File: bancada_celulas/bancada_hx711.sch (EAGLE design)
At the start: 17 parts

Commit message: KK connectors changed from 4mm to 2.54mm
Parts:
- X1, X11, X2, X3, X4, X5: value (none) -> 22-23-2041; device con-molex:KK-156-4 -> con-molex:22-23-2041
- X10, X6, X7, X8, X9: value (none) -> 22-23-2021; device con-molex:KK-156-2 -> con-molex:22-23-2021
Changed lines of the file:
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@@
 <grid distance="0.1" unitdist="inch" unit="inch" style="lines" multiple="1" display="no" altdistance="0.01" altunitdist="inch" altunit="inch"/>
 <layers>
-<layer number="1" name="Top" color="4" fill="1" visible="no" active="no"/>
-<layer number="2" name="Route2" color="1" fill="3" visible="no" active="no"/>
-<layer number="3" name="Route3" color="4" fill="3" visible="no" active="no"/>
-<layer number="4" name="Route4" color="1" fill="4" visible="no" active="no"/>
-<layer number="5" name="Route5" color="4" fill="4" visible="no" active="no"/>
-<layer number="6" name="Route6" color="1" fill="8" visible="no" active="no"/>
-<layer number="7" name="Route7" color="4" fill="8" visible="no" active="no"/>
-<layer number="8" name="Route8" color="1" fill="2" visible="no" active="no"/>
-<layer number="9" name="Route9" color="4" fill="2" visible="no" active="no"/>
-<layer number="10" name="Route10" color="1" fill="7" visible="no" active="no"/>
-<layer number="11" name="Route11" color="4" fill="7" visible="no" active="no"/>
-<layer number="12" name="Route12" color="1" fill="5" visible="no" active="no"/>
-<layer number="13" name="Route13" color="4" fill="5" visible="no" active="no"/>
-<layer number="14" name="Route14" color="1" fill="6" visible="no" active="no"/>
-<layer number="15" name="Route15" color="4" fill="6" visible="no" active="no"/>
-<layer number="16" name="Bottom" color="1" fill="1" visible="no" active="no"/>
-<layer number="17" name="Pads" color="2" fill="1" visible="no" active="no"/>
-<layer number="18" name="Vias" color="2" fill="1" visible="no" active="no"/>
-<layer number="19" name="Unrouted" color="6" fill="1" visible="no" active="no"/>
-<layer number="20" name="Dimension" color="15" fill="1" visible="no" active="no"/>
-<layer number="21" name="tPlace" color="7" fill="1" visible="no" active="no"/>
-<layer number="22" name="bPlace" color="7" fill="1" visible="no" active="no"/>
-<layer number="23" name="tOrigins" color="15" fill="1" visible="no" active="no"/>
-<layer number="24" name="bOrigins" color="15" fill="1" visible="no" active="no"/>
-<layer number="25" name="tNames" color="7" fill="1" visible="no" active="no"/>
-<layer number="26" name="bNames" color="7" fill="1" visible="no" active="no"/>
-<layer number="27" name="tValues" color="7" fill="1" visible="no" active="no"/>
-<layer number="28" name="bValues" color="7" fill="1" visible="no" active="no"/>
+<layer number="1" name="Top" color="4" fill="1" visible="yes" active="no"/>
+<layer number="2" name="Route2" color="1" fill="3" visible="yes" active="no"/>
+<layer number="3" name="Route3" color="4" fill="3" visible="yes" active="no"/>
+<layer number="4" name="Route4" color="1" fill="4" visible="yes" active="no"/>
+<layer number="5" name="Route5" color="4" fill="4" visible="yes" active="no"/>
+<layer number="6" name="Route6" color="1" fill="8" visible="yes" active="no"/>
+<layer number="7" name="Route7" color="4" fill="8" visible="yes" active="no"/>
+<layer number="8" name="Route8" color="1" fill="2" visible="yes" active="no"/>
+<layer number="9" name="Route9" color="4" fill="2" visible="yes" active="no"/>
+<layer number="10" name="Route10" color="1" fill="7" visible="yes" active="no"/>
+<layer number="11" name="Route11" color="4" fill="7" visible="yes" active="no"/>
+<layer number="12" name="Route12" color="1" fill="5" visible="yes" active="no"/>
+<layer number="13" name="Route13" color="4" fill="5" visible="yes" active="no"/>
+<layer number="14" name="Route14" color="1" fill="6" visible="yes" active="no"/>
+<layer number="15" name="Route15" color="4" fill="6" visible="yes" active="no"/>
+<layer number="16" name="Bottom" color="1" fill="1" visible="yes" active="no"/>
+<layer number="17" name="Pads" color="2" fill="1" visible="yes" active="no"/>
+<layer number="18" name="Vias" color="2" fill="1" visible="yes" active="no"/>
+<layer number="19" name="Unrouted" color="6" fill="1" visible="yes" active="no"/>
+<layer number="20" name="Dimension" color="24" fill="1" visible="yes" active="no"/>
+<layer number="21" name="tPlace" color="7" fill="1" visible="yes" active="no"/>
+<layer number="22" name="bPlace" color="7" fill="1" visible="yes" active="no"/>
+<layer number="23" name="tOrigins" color="15" fill="1" visible="yes" active="no"/>
+<layer number="24" name="bOrigins" color="15" fill="1" visible="yes" active="no"/>
+<layer number="25" name="tNames" color="7" fill="1" visible="yes" active="no"/>
+<layer number="26" name="bNames" color="7" fill="1" visible="yes" active="no"/>
+<layer number="27" name="tValues" color="7" fill="1" visible="yes" active="no"/>
+<layer number="28" name="bValues" color="7" fill="1" visible="yes" active="no"/>
 <layer number="29" name="tStop" color="7" fill="3" visible="no" active="no"/>
 <layer number="30" name="bStop" color="7" fill="6" visible="no" active="no"/>
@@
 <layer number="35" name="tGlue" color="7" fill="4" visible="no" active="no"/>
 <layer number="36" name="bGlue" color="7" fill="5" visible="no" active="no"/>
-<layer number="37" name="tTest" color="7" fill="1" visible="no" active="no"/>
-<layer number="38" name="bTest" color="7" fill="1" visible="no" active="no"/>
+<layer number="37" name="tTest" color="7" fill="1" visible="yes" active="no"/>
+<layer number="38" name="bTest" color="7" fill="1" visible="yes" active="no"/>
 <layer number="39" name="tKeepout" color="4" fill="11" visible="no" active="no"/>
 <layer number="40" name="bKeepout" color="1" fill="11" visible="no" active="no"/>
@@
 <layer number="44" name="Drills" color="7" fill="1" visible="no" active="no"/>
 <layer number="45" name="Holes" color="7" fill="1" visible="no" active="no"/>
-<layer number="46" name="Milling" color="3" fill="1" visible="no" active="no"/>
-<layer number="47" name="Measures" color="7" fill="1" visible="no" active="no"/>
-<layer number="48" name="Document" color="7" fill="1" visible="no" active="no"/>
-<layer number="49" name="Reference" color="7" fill="1" visible="no" active="no"/>
-<layer number="51" name="tDocu" color="7" fill="1" visible="no" active="no"/>
-<layer number="52" name="bDocu" color="7" fill="1" visible="no" active="no"/>
+<layer number="46" name="Milling" color="3" fill="1" visible="yes" active="no"/>
+<layer number="47" name="Measures" color="7" fill="1" visible="yes" active="no"/>
+<layer number="48" name="Document" color="7" fill="1" visible="yes" active="no"/>
+<layer number="49" name="Reference" color="7" fill="1" visible="yes" active="no"/>
+<layer number="51" name="tDocu" color="7" fill="1" visible="yes" active="no"/>
+<layer number="52" name="bDocu" color="7" fill="1" visible="yes" active="no"/>
 <layer number="88" name="SimResults" color="9" fill="1" visible="yes" active="yes"/>
 <layer number="89" name="SimProbes" color="9" fill="1" visible="yes" active="yes"/>
@@
 <part name="U$5" library="HX711" deviceset="HX711-1" device=""/>
 <part name="U$6" library="HX711" deviceset="HX711-1" device=""/>
-<part name="X1" library="con-molex" library_urn="urn:adsk.eagle:library:165" deviceset="KK-156-4" device=""/>
-<part name="X2" library="con-molex" library_urn="urn:adsk.eagle:library:165" deviceset="KK-156-4" device=""/>
-<part name="X3" library="con-molex" library_urn="urn:adsk.eagle:library:165" deviceset="KK-156-4" device=""/>
-<part name="X4" library="con-molex" library_urn="urn:adsk.eagle:library:165" deviceset="KK-156-4" device=""/>
-<part name="X5" library="con-molex" library_urn="urn:adsk.eagle:library:165" deviceset="KK-156-4" device=""/>
-<part name="X6" library="con-molex" library_urn="urn:adsk.eagle:library:165" deviceset="KK-156-2" device=""/>
-<part name="X7" library="con-molex" library_urn="urn:adsk.eagle:library:165" deviceset="KK-156-2" device=""/>
-<part name="X8" library="con-molex" library_urn="urn:adsk.eagle:library:165" deviceset="KK-156-2" device=""/>
-<part name="X9" library="con-molex" library_urn="urn:adsk.eagle:library:165" deviceset="KK-156-2" device=""/>
-<part name="X10" library="con-molex" library_urn="urn:adsk.eagle:library:165" deviceset="KK-156-2" device=""/>
+<part name="X1" library="con-molex" library_urn="urn:adsk.eagle:library:165" deviceset="22-23-2041" device=""/>
+<part name="X2" library="con-molex" library_urn="urn:adsk.eagle:library:165" deviceset="22-23-2041" device=""/>
+<part name="X3" library="con-molex" library_urn="urn:adsk.eagle:library:165" deviceset="22-23-2041" device=""/>
+<part name="X4" library="con-molex" library_urn="urn:adsk.eagle:library:165" deviceset="22-23-2041" device=""/>
+<part name="X5" library="con-molex" library_urn="urn:adsk.eagle:library:165" deviceset="22-23-2041" device=""/>
+<part name="X6" library="con-molex" library_urn="urn:adsk.eagle:library:165" deviceset="22-23-2021" device=""/>
+<part name="X7" library="con-molex" library_urn="urn:adsk.eagle:library:165" deviceset="22-23-2021" device=""/>
+<part name="X8" library="con-molex" library_urn="urn:adsk.eagle:library:165" deviceset="22-23-2021" device=""/>
+<part name="X9" library="con-molex" library_urn="urn:adsk.eagle:library:165" deviceset="22-23-2021" device=""/>
+<part name="X10" library="con-molex" library_urn="urn:adsk.eagle:library:165" deviceset="22-23-2021" device=""/>
 <part name="GND7" library="supply1" library_urn="urn:adsk.eagle:library:371" deviceset="GND" device=""/>
 <part name="GND8" library="supply1" library_urn="urn:adsk.eagle:library:371" deviceset="GND" device=""/>
@@
 <part name="P+7" library="supply1" library_urn="urn:adsk.eagle:library:371" deviceset="VCC" device=""/>
 <part name="GND12" library="supply1" library_urn="urn:adsk.eagle:library:371" deviceset="GND" device=""/>
-<part name="X11" library="con-molex" library_urn="urn:adsk.eagle:library:165" deviceset="KK-156-4" device=""/>
+<part name="X11" library="con-molex" library_urn="urn:adsk.eagle:library:165" deviceset="22-23-2041" device=""/>
 </parts>
 <sheets>

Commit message: Name A4 and A5 lines
A4 and A5 lines were hardwired. They are now named A4 and A5.
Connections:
- net N$21 renamed A5
- net N$22 renamed A4
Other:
- moved on the sheet: X11-1, X11-2, X11-3, X11-4

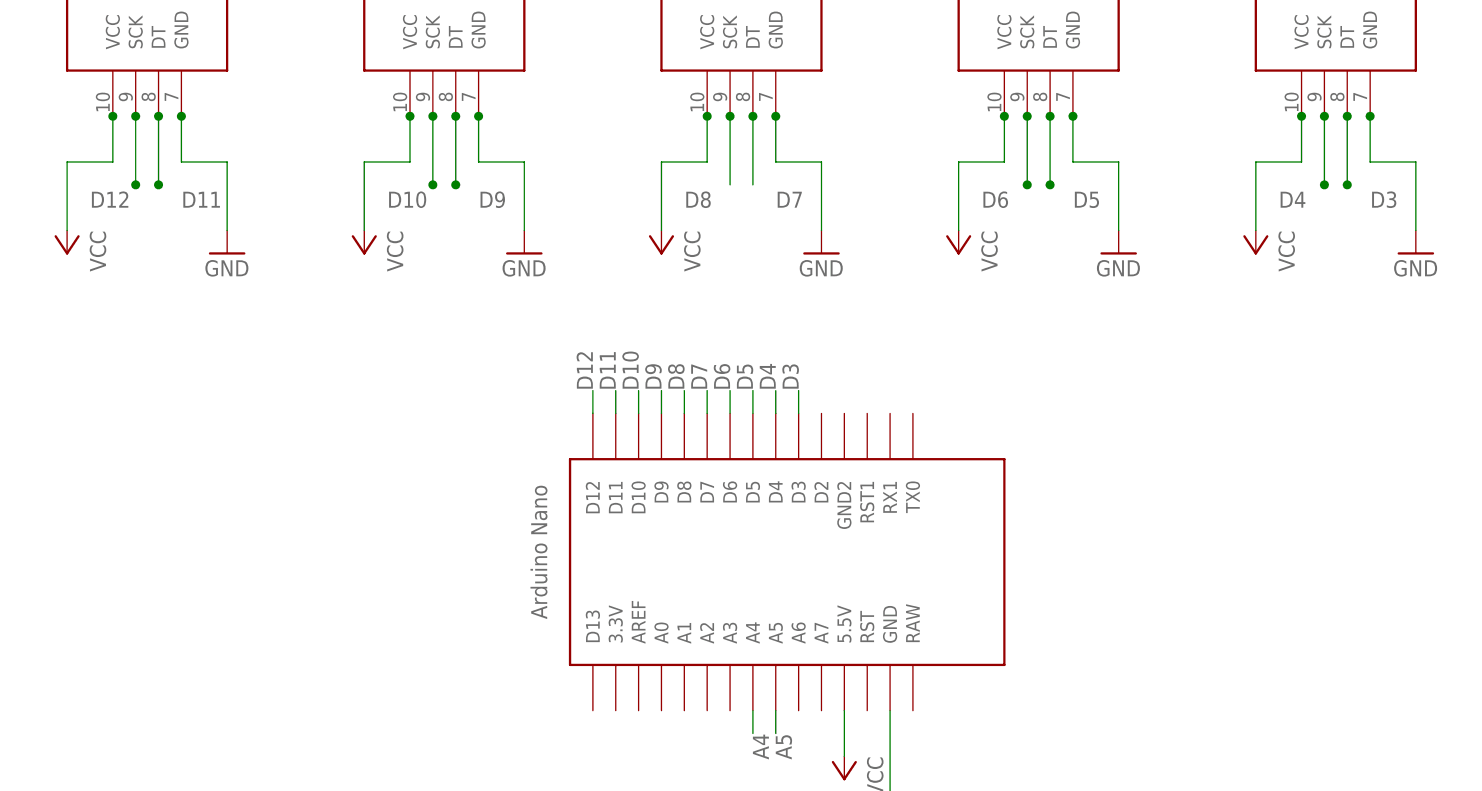
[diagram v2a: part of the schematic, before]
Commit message: Add jumpers (or 0ohm resistors)
In previous design, some ground planes were unconnected to each other. It was meant to be added jumper wires after production.

This commit changes this to actual jumpers, with pins, so they don't need to be soldered from bottom, but can actually be placed on top, like any other through-hole component. 0ohm through-hole resistors can also be used.
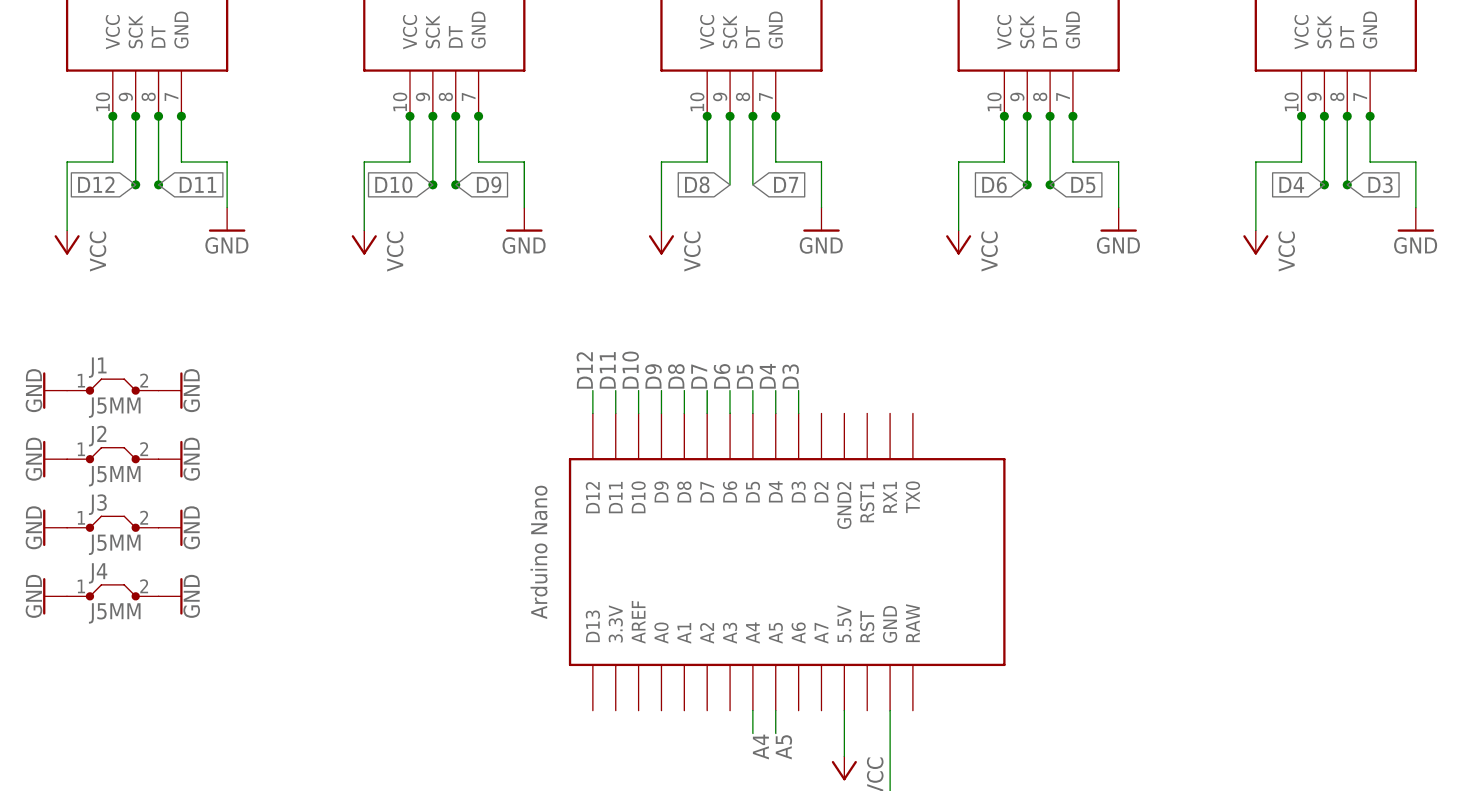
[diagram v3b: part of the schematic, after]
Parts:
- added J1, J2, J3, J4: J5MM, jumper:J5MM
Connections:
- net GND: now also J1.1, J1.2, J2.1, J2.2, J3.1, J3.2, J4.1, J4.2
